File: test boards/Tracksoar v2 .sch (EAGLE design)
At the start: 48 parts, among them IC1 BME280, IC2 74AHC1G125DBV, Y1 16MHZ

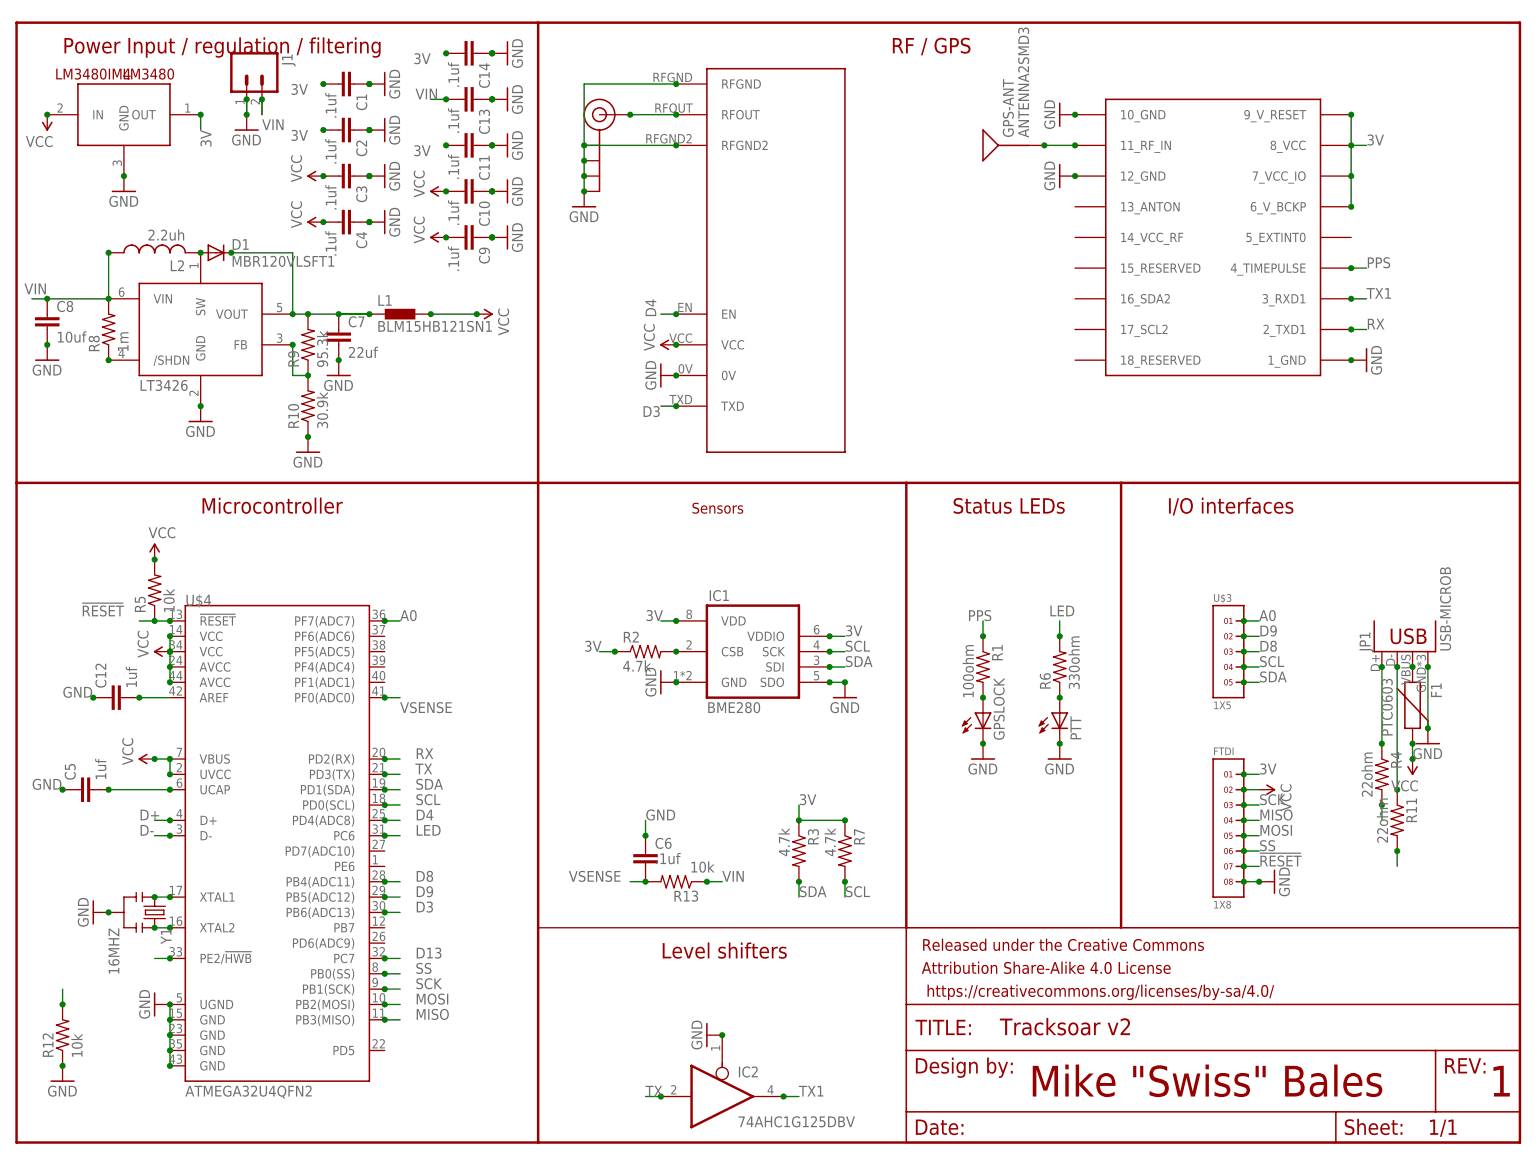
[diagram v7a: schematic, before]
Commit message: Silkscreen cleanup and additional analog pin
removed as many silkscreen keep out errors as possible. Added a
breakout for analog pin A1 to the bottom header.
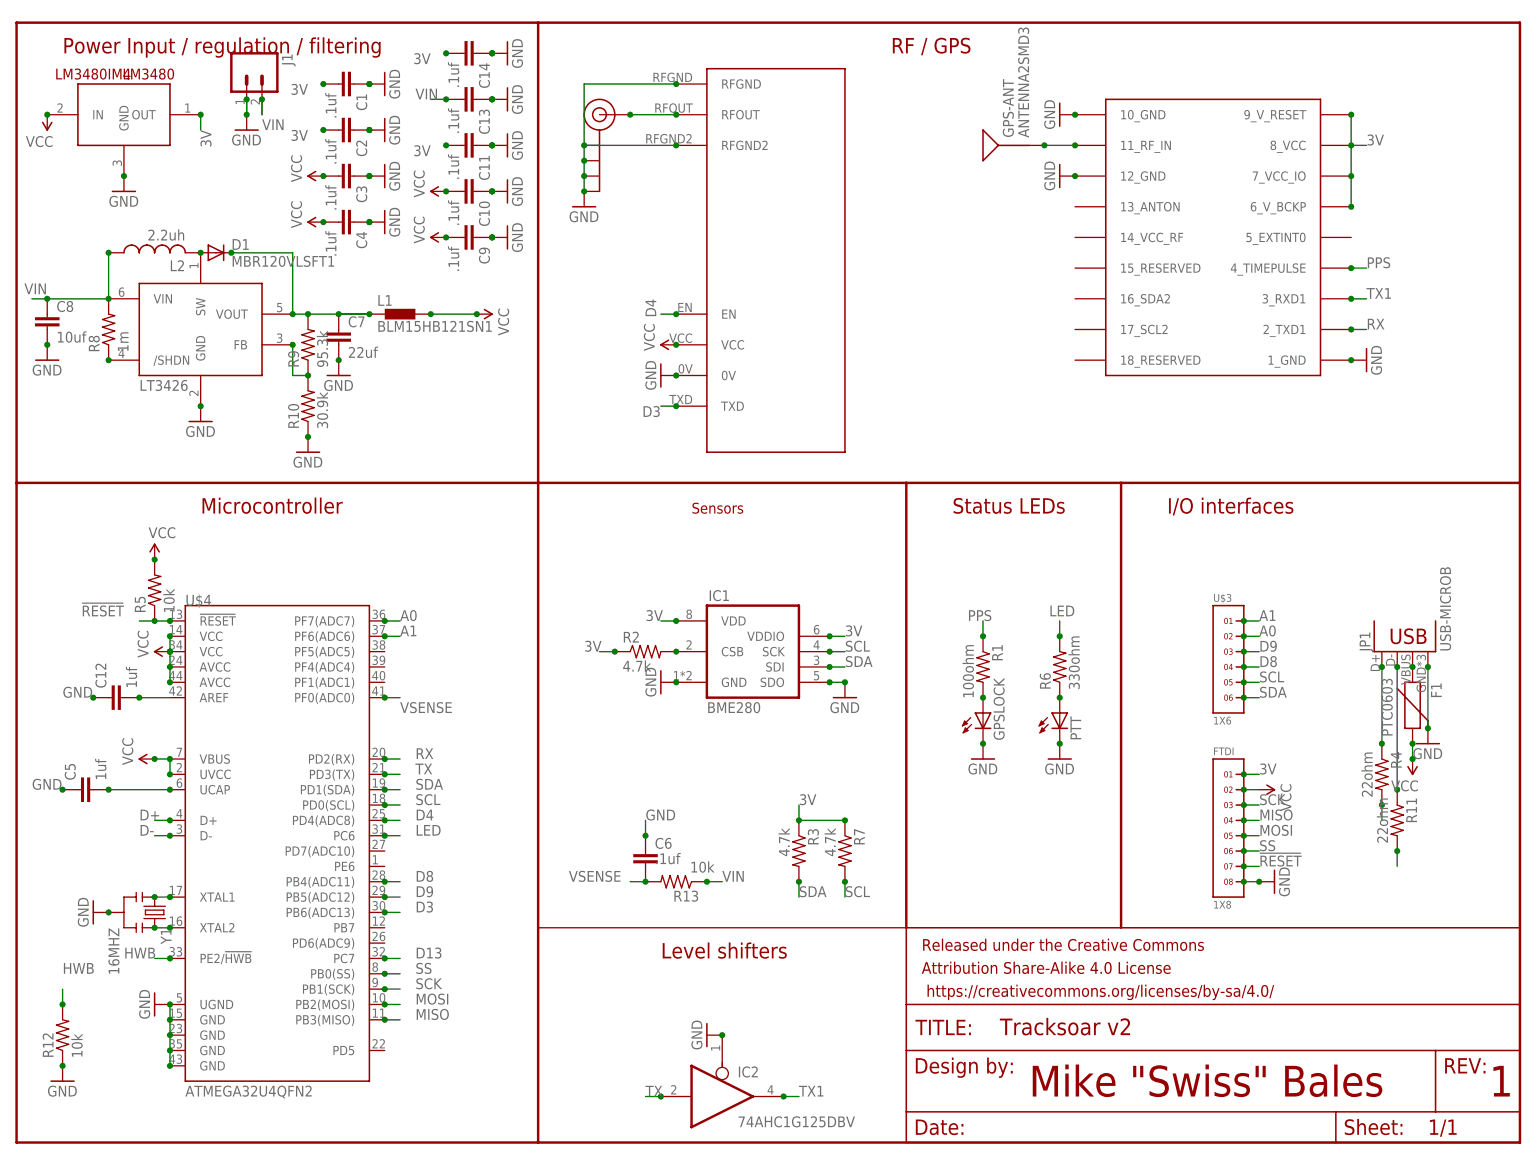
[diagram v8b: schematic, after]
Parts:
- U$3: value 1X5 -> 1X6; device headers(2mm):1X5 -> headers(2mm):1X6
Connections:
- new net A1: U$3.1, U$4.PF6(ADC6)
- net A0: now also U$3.2; no longer U$3.1
- net D8: now also U$3.4; no longer U$3.3
- net D9: now also U$3.3; no longer U$3.2
- net SCL: now also U$3.5; no longer U$3.4
- net SDA: now also U$3.6; no longer U$3.5
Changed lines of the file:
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@@
 <part name="SUPPLY16" library="SparkFun-Aesthetics" deviceset="VCC" device=""/>
 <part name="C5" library="SparkFun-Capacitors" deviceset="CAP" device="0402-CAP" value="1uf"/>
-<part name="U$3" library="headers(2mm)" deviceset="1X5" device=""/>
+<part name="U$3" library="headers(2mm)" deviceset="1X6" device=""/>
 <part name="L1" library="inductors" deviceset="BLM15H" device="" technology="B121SN1"/>
 <part name="R13" library="adafruit" deviceset="R-US_" device="R0402" value="10k"/>
@@
 <instance part="SUPPLY16" gate="G$1" x="22.86" y="63.5" rot="R90"/>
 <instance part="C5" gate="G$1" x="12.7" y="58.42" rot="R90"/>
-<instance part="U$3" gate="G$1" x="200.66" y="81.28"/>
+<instance part="U$3" gate="G$1" x="200.66" y="78.74"/>
 <instance part="L1" gate="G$1" x="63.5" y="137.16"/>
 <instance part="R13" gate="G$1" x="109.22" y="43.18" smashed="yes" rot="R180">
@@
 </segment>
 <segment>
+<pinref part="U$3" gate="G$1" pin="6"/>
+<wire x1="203.2" y1="73.66" x2="205.74" y2="73.66" width="0.1524" layer="91"/>
+<label x="205.74" y="73.66" size="1.778" layer="95"/>
+<junction x="203.2" y="73.66"/>
+</segment>
+</net>
+<net name="SCL" class="0">
+<segment>
+<wire x1="137.16" y1="81.28" x2="134.62" y2="81.28" width="0.1524" layer="91"/>
+<label x="137.16" y="81.28" size="1.778" layer="95"/>
+<pinref part="IC1" gate="G$1" pin="SCK"/>
+<junction x="134.62" y="81.28"/>
+</segment>
+<segment>
+<pinref part="R7" gate="G$1" pin="2"/>
+<wire x1="137.16" y1="43.18" x2="137.16" y2="40.64" width="0.1524" layer="91"/>
+<label x="137.16" y="40.64" size="1.778" layer="95"/>
+<junction x="137.16" y="43.18"/>
+</segment>
+<segment>
+<wire x1="60.96" y1="55.88" x2="63.5" y2="55.88" width="0.1524" layer="91"/>
+<pinref part="U$4" gate="G$1" pin="PD0(SCL)"/>
+<junction x="60.96" y="55.88"/>
+<label x="66.04" y="55.88" size="1.778" layer="95"/>
+</segment>
+<segment>
 <pinref part="U$3" gate="G$1" pin="5"/>
 <wire x1="203.2" y1="76.2" x2="205.74" y2="76.2" width="0.1524" layer="91"/>
 <junction x="203.2" y="76.2"/>
 <label x="205.74" y="76.2" size="1.778" layer="95"/>
-</segment>
-</net>
-<net name="SCL" class="0">
-<segment>
-<wire x1="137.16" y1="81.28" x2="134.62" y2="81.28" width="0.1524" layer="91"/>
-<label x="137.16" y="81.28" size="1.778" layer="95"/>
-<pinref part="IC1" gate="G$1" pin="SCK"/>
-<junction x="134.62" y="81.28"/>
-</segment>
-<segment>
-<pinref part="R7" gate="G$1" pin="2"/>
-<wire x1="137.16" y1="43.18" x2="137.16" y2="40.64" width="0.1524" layer="91"/>
-<label x="137.16" y="40.64" size="1.778" layer="95"/>
-<junction x="137.16" y="43.18"/>
-</segment>
-<segment>
-<wire x1="60.96" y1="55.88" x2="63.5" y2="55.88" width="0.1524" layer="91"/>
-<pinref part="U$4" gate="G$1" pin="PD0(SCL)"/>
-<junction x="60.96" y="55.88"/>
-<label x="66.04" y="55.88" size="1.778" layer="95"/>
-</segment>
-<segment>
-<pinref part="U$3" gate="G$1" pin="4"/>
-<wire x1="203.2" y1="78.74" x2="205.74" y2="78.74" width="0.1524" layer="91"/>
-<junction x="203.2" y="78.74"/>
-<label x="205.74" y="78.74" size="1.778" layer="95"/>
 </segment>
 </net>
@@
 </segment>
 <segment>
+<pinref part="U$3" gate="G$1" pin="4"/>
+<wire x1="203.2" y1="78.74" x2="205.74" y2="78.74" width="0.1524" layer="91"/>
+<junction x="203.2" y="78.74"/>
+<label x="205.74" y="78.74" size="1.778" layer="95"/>
+</segment>
+</net>
+<net name="D9" class="0">
+<segment>
+<pinref part="U$4" gate="G$1" pin="PB5(ADC12)"/>
+<wire x1="60.96" y1="40.64" x2="63.5" y2="40.64" width="0.1524" layer="91"/>
+<junction x="60.96" y="40.64"/>
+<label x="66.04" y="40.64" size="1.778" layer="95"/>
+</segment>
+<segment>
 <pinref part="U$3" gate="G$1" pin="3"/>
 <wire x1="203.2" y1="81.28" x2="205.74" y2="81.28" width="0.1524" layer="91"/>
@@
 </segment>
 </net>
-<net name="D9" class="0">
-<segment>
-<pinref part="U$4" gate="G$1" pin="PB5(ADC12)"/>
-<wire x1="60.96" y1="40.64" x2="63.5" y2="40.64" width="0.1524" layer="91"/>
-<junction x="60.96" y="40.64"/>
-<label x="66.04" y="40.64" size="1.778" layer="95"/>
+<net name="D13" class="0">
+<segment>
+<pinref part="U$4" gate="G$1" pin="PC7"/>
+<wire x1="60.96" y1="30.48" x2="63.5" y2="30.48" width="0.1524" layer="91"/>
+<junction x="60.96" y="30.48"/>
+<label x="66.04" y="30.48" size="1.778" layer="95"/>
+</segment>
+</net>
+<net name="A0" class="0">
+<segment>
+<pinref part="U$4" gate="G$1" pin="PF7(ADC7)"/>
+<wire x1="60.96" y1="86.36" x2="63.5" y2="86.36" width="0.1524" layer="91"/>
+<junction x="60.96" y="86.36"/>
+<label x="63.5" y="86.36" size="1.778" layer="95"/>
 </segment>
 <segment>
@@
 <junction x="203.2" y="83.82"/>
 <label x="205.74" y="83.82" size="1.778" layer="95"/>
-</segment>
-</net>
-<net name="D13" class="0">
-<segment>
-<pinref part="U$4" gate="G$1" pin="PC7"/>
-<wire x1="60.96" y1="30.48" x2="63.5" y2="30.48" width="0.1524" layer="91"/>
-<junction x="60.96" y="30.48"/>
-<label x="66.04" y="30.48" size="1.778" layer="95"/>
-</segment>
-</net>
-<net name="A0" class="0">
-<segment>
-<pinref part="U$4" gate="G$1" pin="PF7(ADC7)"/>
-<wire x1="60.96" y1="86.36" x2="63.5" y2="86.36" width="0.1524" layer="91"/>
-<junction x="60.96" y="86.36"/>
-<label x="63.5" y="86.36" size="1.778" layer="95"/>
-</segment>
-<segment>
-<pinref part="U$3" gate="G$1" pin="1"/>
-<wire x1="203.2" y1="86.36" x2="205.74" y2="86.36" width="0.1524" layer="91"/>
-<junction x="203.2" y="86.36"/>
-<label x="205.74" y="86.36" size="1.778" layer="95"/>
 </segment>
 </net>
@@
 <wire x1="25.4" y1="30.48" x2="22.86" y2="30.48" width="0.1524" layer="91"/>
 <junction x="25.4" y="30.48"/>
+<label x="17.78" y="30.48" size="1.778" layer="95"/>
 </segment>
 <segment>
@@
 <wire x1="7.62" y1="22.86" x2="7.62" y2="25.4" width="0.1524" layer="91"/>
 <junction x="7.62" y="22.86"/>
-</segment>
-</net>
+<label x="7.62" y="27.94" size="1.778" layer="95"/>
+</segment>
+</net>
+<net name="A1" class="0">
+<segment>
+<pinref part="U$3" gate="G$1" pin="1"/>
+<wire x1="203.2" y1="86.36" x2="205.74" y2="86.36" width="0.1524" layer="91"/>
+<junction x="203.2" y="86.36"/>
+<label x="205.74" y="86.36" size="1.778" layer="95"/>
+</segment>
+<segment>
+<pinref part="U$4" gate="G$1" pin="PF6(ADC6)"/>
+<wire x1="60.96" y1="83.82" x2="63.5" y2="83.82" width="0.1524" layer="91"/>
+<junction x="60.96" y="83.82"/>
+<label x="63.5" y="83.82" size="1.778" layer="95"/>
+</segment>
+</net>
